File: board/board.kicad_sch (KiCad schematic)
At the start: 18 parts, among them J1 24pin FPC, 0.5mm, Q1 Si1308EDL

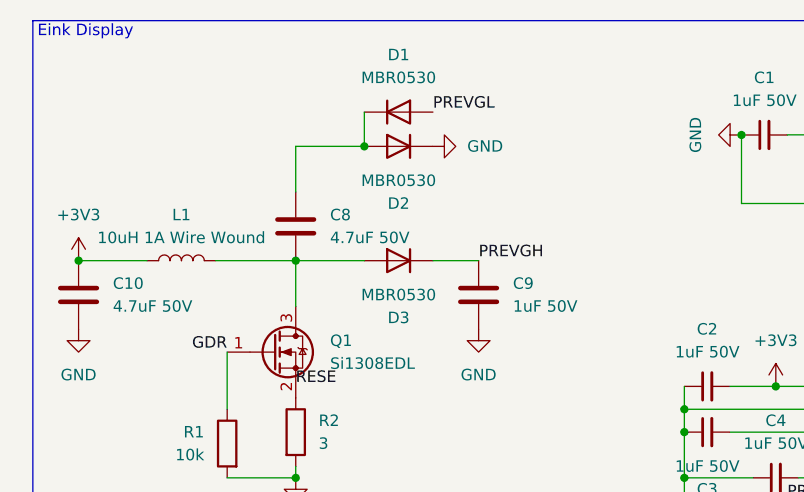
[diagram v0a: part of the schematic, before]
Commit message: Start assigning footprints
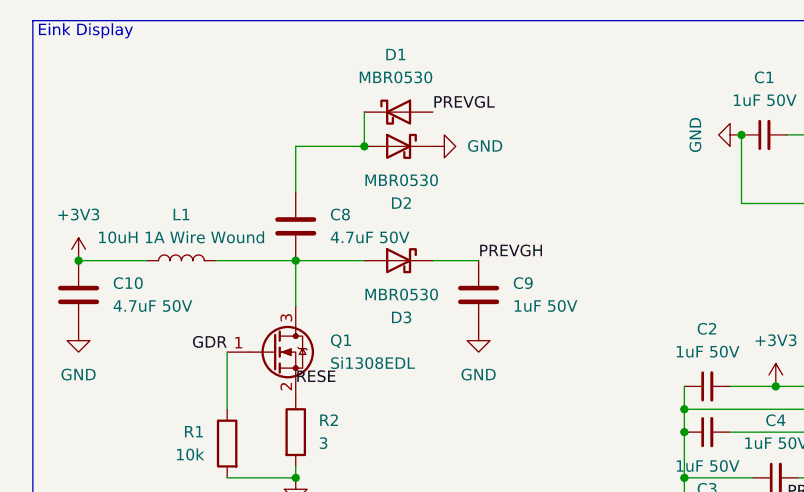
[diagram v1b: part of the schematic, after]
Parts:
- removed D1, D2, D3: MBR0530, symbol Device:D
- added D1, D2, D3: MBR0530, Diode_SMD:D_SOD-123, symbol Diode:MBR0530
- C1, C10, C2, C3, C4, C5, C6, C7, C8, C9: footprint (none) -> Capacitor_SMD:C_0805_2012Metric_Pad1.18x1.45mm_HandSolder
- J1: footprint (none) -> Connector_FFC-FPC:JUSHUO_AFA07-S23FCA-00_1x23-1MP_P1.0mm_Horizontal
- R1, R2: footprint (none) -> Resistor_SMD:R_0805_2012Metric_Pad1.20x1.40mm_HandSolder
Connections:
- net GND: now also D2.1 (K)
- net PREVGH: now also D3.1 (K)
- net PREVGL: now also D1.2 (A)
- net at C8.2, L1.2, Q1.3 (D): now also D3.2 (A)
- net at C8.1: now also D1.1 (K), D2.2 (A)

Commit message: Continue work
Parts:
- added H1, H2, H3, H4: MountingHole, MountingHole:MountingHole_2.2mm_M2, symbol Mechanical:MountingHole
- J1: footprint Connector_FFC-FPC:JUSHUO_AFA07-S23FCA-00_1x23-1MP_P1.0mm_Horizontal -> AFC07-S24ECA-00:AFC07S24ECA00
- L1: footprint (none) -> Inductor_SMD:L_0603_1608Metric_Pad1.05x0.95mm_HandSolder

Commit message: Hello Power!
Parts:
- added C11, C12: 1uF, Capacitor_SMD:C_0805_2012Metric_Pad1.18x1.45mm_HandSolder, symbol Device:C
- added C13: 10uF, Capacitor_SMD:C_0805_2012Metric_Pad1.18x1.45mm_HandSolder, symbol Device:C
- added D4: C8678, symbol Device:D
- added D5: RED, symbol Device:LED
- added D6: GREEN, symbol Device:LED
- added J2: USB_C_Receptacle_USB2.0_14P, symbol Connector:USB_C_Receptacle_USB2.0_14P
- added J3: Conn_01x02, symbol Connector_Generic:Conn_01x02
- added Q2: AO3401A, Package_TO_SOT_SMD:SOT-23, symbol Transistor_FET:AO3401A
- added R3, R4: 5.1K, Resistor_SMD:R_0805_2012Metric_Pad1.20x1.40mm_HandSolder, symbol Device:R
- added R5: 10k, Resistor_SMD:R_0805_2012Metric_Pad1.20x1.40mm_HandSolder, symbol Device:R
- added R6: 5k, Resistor_SMD:R_0805_2012Metric_Pad1.20x1.40mm_HandSolder, symbol Device:R
- added R7: 4.7k, Resistor_SMD:R_0805_2012Metric_Pad1.20x1.40mm_HandSolder, symbol Device:R
- added R8: 1k, Resistor_SMD:R_0805_2012Metric_Pad1.20x1.40mm_HandSolder, symbol Device:R
- added U1: XC6206PxxxMR, Package_TO_SOT_SMD:SOT-23-3, symbol Regulator_Linear:XC6206PxxxMR
- added U2: TP4057, Package_TO_SOT_SMD:TSOT-23-6, symbol Battery_Management:TP4057
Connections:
- net GND: now also C13.2, J2.A1 (GND), J2.A12 (GND), J2.B1 (GND), J2.B12 (GND), J2.S1 (SHIELD), J3.2 (Pin_2), R3.2, R4.2, R5.2
- new net: C11.1, D4.1 (K), Q2.2 (S), U1.3 (VI)
- new net: D5.2 (A), D6.2 (A), R8.2
- new net: R6.1, U2.6 (PROG)
- new net: R6.2, U2.2 (GND)
- new net: J2.B5 (CC2), R4.1
- new net: J2.A5 (CC1), R3.1
- new net: D6.1 (K), U2.5 (STDBY)
- new net: C11.2, C12.2, U1.1 (GND)
- new net: D5.1 (K), U2.1 (~{CHRG})
- new net D+: J2.A6 (D+), J2.B6 (D+)
- new net D-: J2.A7 (D-), J2.B7 (D-)
- new net VBAT: C13.1, J3.1 (Pin_1), Q2.3 (D), R7.2, U2.3 (BAT)
- new net VCC: C12.1, U1.2 (VO)
- new net VUSB: D4.2 (A), J2.A4 (VBUS), J2.A9 (VBUS), J2.B4 (VBUS), J2.B9 (VBUS), Q2.1 (G), R5.1, R7.1, R8.1, U2.4 (V_{CC})
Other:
- note added: "Power"
